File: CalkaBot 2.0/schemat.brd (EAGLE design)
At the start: 94.2 x 84.6 mm, 57 parts, among them IC1 TB6612FNG, IC2 LM339D, IC3 7806DT, Q1 16MHz

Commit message: end 3x
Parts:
- moved R11 14.4 mm to (8.20, 2.60)
- moved U$3 14.4 mm to (1.30, 2.50)
- moved R14 13.8 mm to (67.4, 2.60)
- moved U$2 13.8 mm to (74.4, 2.50)
- moved C6 13.6 mm to (23.6, 46.9)
- moved IC1 13.5 mm to (57.5, 57.9)
- moved LED3 13.5 mm to (65.1, 28.4)
- moved R10 13.5 mm to (65.3, 19.4)
- moved R8 13.5 mm to (72.1, 54.3)
- moved LED4 13.5 mm to (65.1, 24.2)
- moved R13 13.5 mm to (65.3, 21.5)
- moved C2 13.5 mm to (37.4, 9.72)
- moved C3 13.5 mm to (10.4, 43.1)
- moved IC3 13.5 mm to (15.0, 52.0)
- moved JP1 13.5 mm to (17.5, 57.2)
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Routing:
- net BO1: track 57.1 -> 105.2 mm
- net GND: track 481.3 -> 499.6 mm, vias 7 -> 8
- net VCC: track 432.6 -> 449.6 mm
- net FL3: track 43.5 -> 35.0 mm
- net I/O1: track 15.0 -> 8.22 mm
- net N$19: track 4.85 -> 10.8 mm
- net I/O2: track 14.5 -> 9.33 mm
- net AO2: track 19.6 -> 15.4 mm
- net N$1: track 8.38 -> 4.66 mm
- net I/O3: track 14.1 -> 10.5 mm
- net BO2: track 57.2 -> 59.7 mm
- net I/O4: track 13.6 -> 11.6 mm
- net I/O9: track 11.8 -> 12.9 mm
- net I/O6: track 12.7 -> 13.8 mm
- net S1: track 59.0 -> 59.6 mm
- added copper zone on layer 1, net N$3
- added copper zone on layer 16, net N$5
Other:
- board size 94.2 x 84.6 mm -> 76.8 x 68.7 mm
- board text added: "+"
- board text added: "A0"
- board text added: "A5"
- board text added: "C"
- board text added: "CałkaBot2.0"

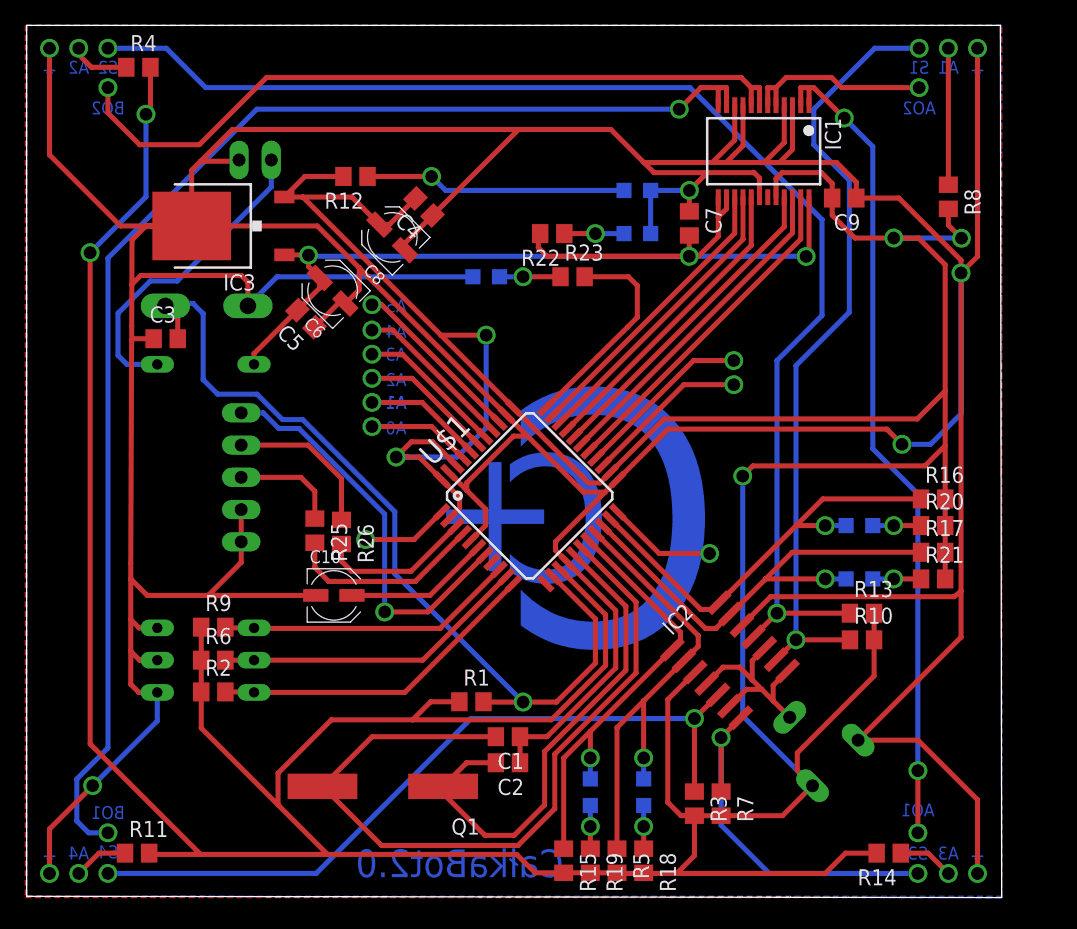
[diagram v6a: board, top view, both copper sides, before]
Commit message: poprawki wprowadzone, zmiana dipa z 3 na 4, przesunięcie włącznika zasilania
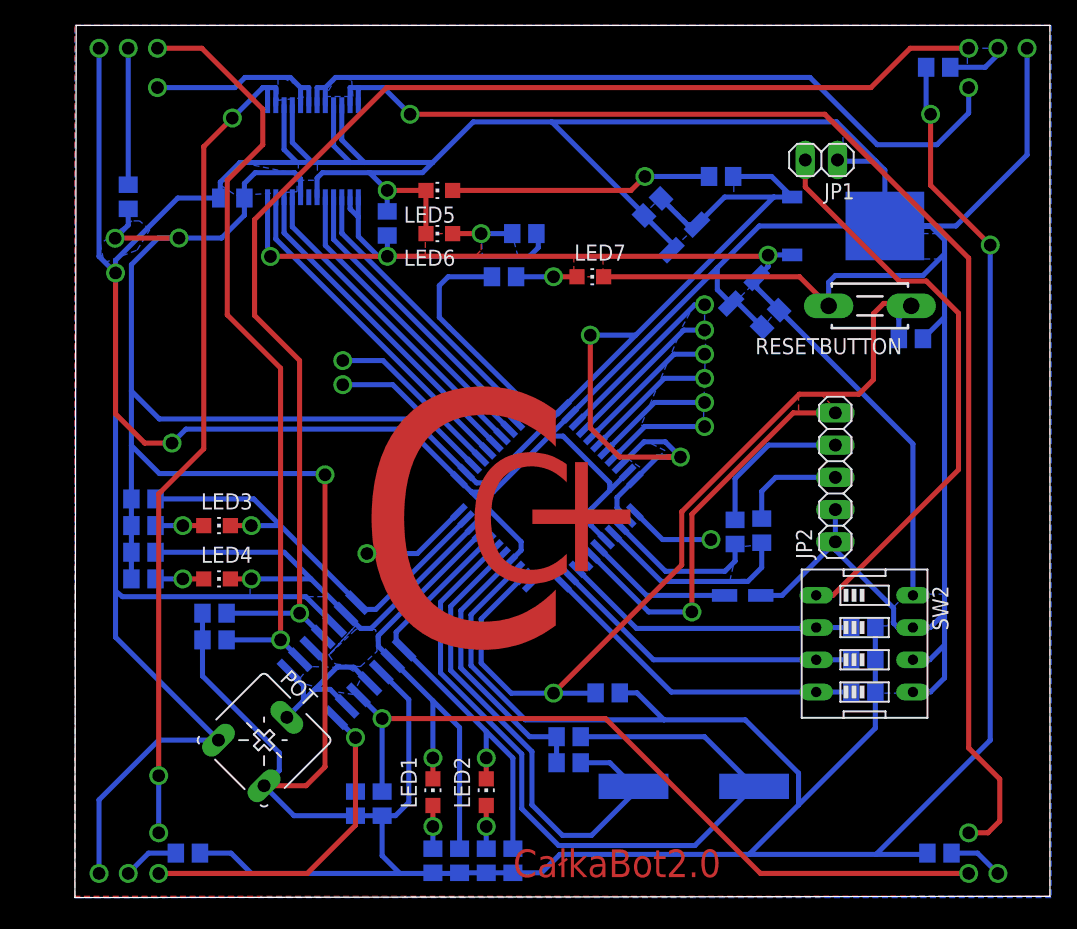
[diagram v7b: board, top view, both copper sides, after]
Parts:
- removed SW1: (no value), special:EDG-01
- removed U$2, U$3, U$4, U$5: (no value), untitled:GND@1
- SW2: device special:EDG-03 -> special:EDG-04
- moved R8 64.6 mm to (7.50, 54.3), flipped to the bottom
- moved R11 63.2 mm to (71.4, 2.60), flipped to the bottom
- moved R4 63.0 mm to (71.3, 64.5), flipped to the bottom
- moved R16 62.2 mm to (8.70, 30.5), flipped to the bottom
- moved R17 62.2 mm to (8.70, 26.3), flipped to the bottom
- moved R20 62.2 mm to (8.70, 28.4), flipped to the bottom
- moved R21 62.2 mm to (8.70, 24.2), flipped to the bottom
- moved C3 58.7 mm to (69.2, 43.1), flipped to the bottom
- moved R14 55.2 mm to (12.2, 2.60), flipped to the bottom
- moved RESETBUTTON 52.2 mm to (65.9, 45.7), flipped to the top
- moved SW2 51.9 mm to (65.5, 19.1), flipped to the top
- moved R2 51.2 mm to (65.4, 15.3), flipped to the bottom
- moved R6 51.2 mm to (65.4, 17.8), flipped to the bottom
- moved R9 51.2 mm to (65.4, 20.4), flipped to the bottom
- moved R10 51.0 mm to (14.3, 19.4), flipped to the bottom
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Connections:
- net GND: now also SW2.7; no longer SW2.4
- net MISO: now also SW2.4; no longer SW2.3
- net MOSI: now also SW2.3; no longer SW2.2
- net PIN: now also SW2.1; no longer SW1.1
- net SCK: now also SW2.2; no longer SW2.1
- net VM: now also SW2.8; no longer SW1.2
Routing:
- net VM: track 79.9 -> 101.1 mm
- net PIN: track 25.0 -> 46.0 mm
- net GND: track 499.6 -> 482.6 mm, vias 8 -> 6
- net VCC: track 449.6 -> 450.7 mm
- net RST: track 68.5 -> 67.7 mm
- added copper zone on layer 16, net N$14
- added copper zone on layer 16, net N$18
- added copper zone on layer 16, net N$20
- added copper zone on layer 16, net N$21
- added copper zone on layer 16, net N$22
- added copper zone on layer 16, net N$24
- added copper zone on layer 1, net N$25
- added copper zone on layer 16, net N$26
- added copper zone on layer 16, net N$28
- added copper zone on layer 16, net N$3
- added copper zone on layer 16, net N$32
- added copper zone on layer 16, net N$33
- added copper zone on layer 16, net N$34
- added copper zone on layer 16, net N$35
- added copper zone on layer 16, net N$36
- added copper zone on layer 16, net N$37
- added copper zone on layer 16, net N$38
- added copper zone on layer 16, net N$39
- added copper zone on layer 16, net N$40
- added copper zone on layer 1, net N$41
- added copper zone on layer 1, net N$42
- added copper zone on layer 16, net N$43
- added copper zone on layer 1, net N$5
- added copper zone on layer 16, net N$6
- added copper zone on layer 16, net N$8
- removed copper zone on layer 1, net N$3
- removed copper zone on layer 16, net N$5
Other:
- outline, holes or cut-outs redrawn
- board text removed: "A0"
- board text removed: "A1"
- board text removed: "A2"
- board text removed: "A3"
- board text removed: "A4"
- board text removed: "A5"
- board text removed: "AO1"
- board text removed: "AO2"
- board text removed: "BO1"
- board text removed: "BO2"
- board text removed: "S1"
- board text removed: "S2"
- board text removed: "S3"
- board text removed: "S4"

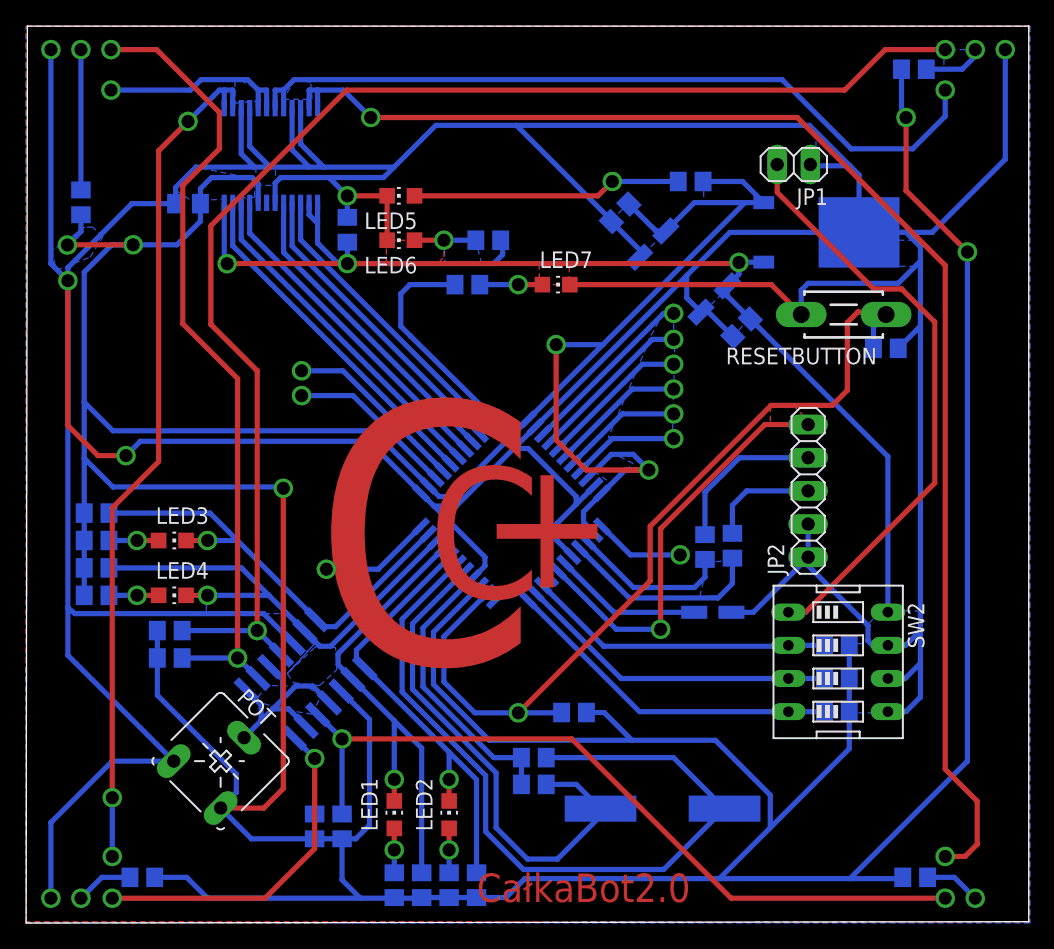
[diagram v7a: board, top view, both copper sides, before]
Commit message: dodałem gniazdo B, włącznik przyłączony z trybami
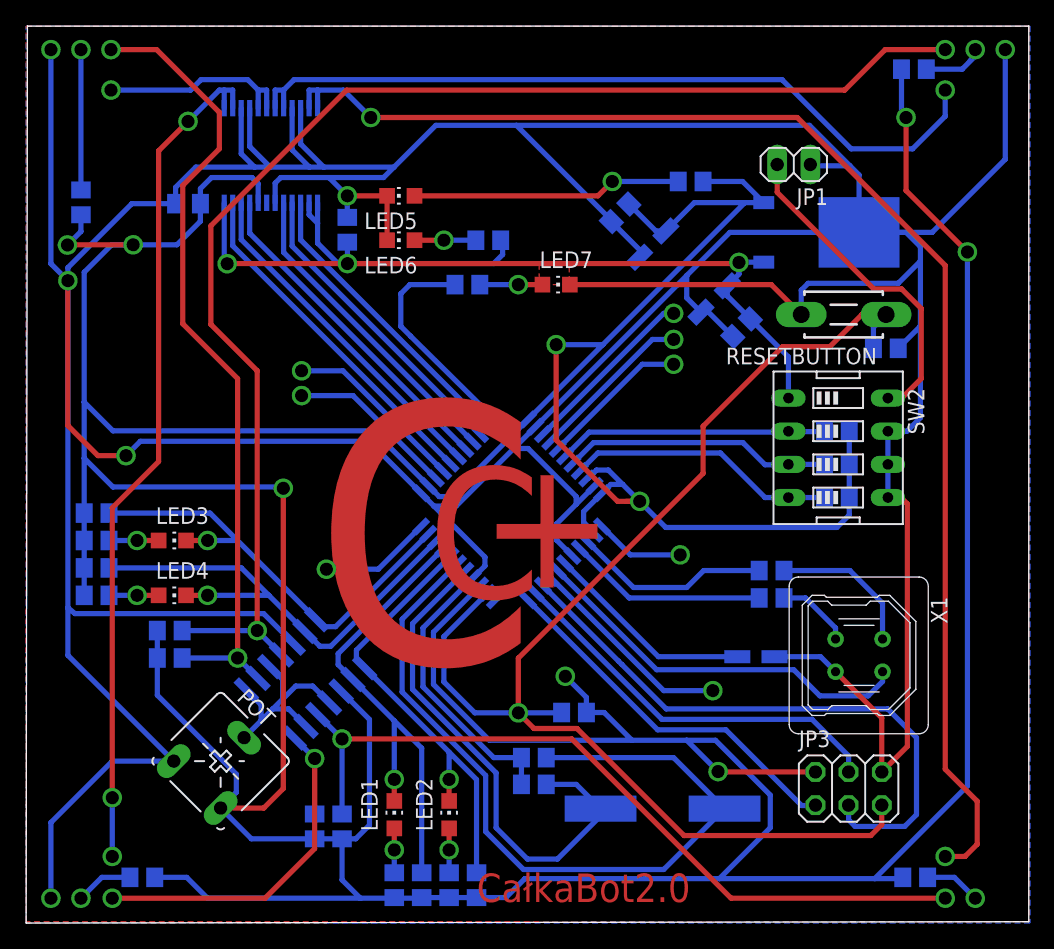
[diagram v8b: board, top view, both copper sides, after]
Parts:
- removed JP2: (no value), pinhead:1X05
- added JP3: (no value), pinhead:2X03
- added X1: MINI-USB_4P-85-32004-40X, con-cypressindustries:85-32004-40X
- moved R6 16.4 mm to (65.4, 34.2)
- moved R2 16.4 mm to (65.4, 31.7)
- moved R9 16.4 mm to (65.4, 36.8)
- moved SW2 16.4 mm to (65.5, 35.5)
- moved R26 5.41 mm to (60.4, 26.1), turned to 0 degrees
- moved R25 5.00 mm to (60.4, 24.0), turned to 0 degrees
- moved C10 4.74 mm to (59.2, 19.5)
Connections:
- new net I/O13: U$1.8
- net GND: now also JP3.6, X1.4; no longer JP2.1, JP2.2
- net I/O1: now also R2.2, SW2.4
- net I/O2: now also R6.2, SW2.3
- net I/O3: now also R9.2, SW2.2
- net MISO: now also JP3.1; no longer R2.2, SW2.4
- net MOSI: now also JP3.4; no longer R6.2, SW2.3
- net N$11: now also X1.2; no longer JP2.4
- net N$12: now also X1.3; no longer JP2.3
- net PIN: now also SW2.8; no longer SW2.1
- net RST: now also JP3.5
- net SCK: now also JP3.3; no longer R9.2, SW2.2
- net VBUS: now also X1.1; no longer JP2.5
- net VCC: now also JP3.2
- net VM: now also SW2.1; no longer SW2.8
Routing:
- net RST: track 67.7 -> 100.1 mm
- net SCK: track 24.0 -> 46.3 mm
- net PIN: track 46.0 -> 25.4 mm
- net VM: track 101.1 -> 81.5 mm
- net VCC: track 450.7 -> 468.6 mm, vias 7 -> 9
- net I/O13: track 0.00 -> 16.0 mm, vias 0 -> 1
- net I/O1: track 8.22 -> 20.7 mm, vias 1 -> 0
- net I/O2: track 9.33 -> 20.7 mm, vias 1 -> 0
- net I/O3: track 10.5 -> 20.8 mm, vias 1 -> 0
- net MOSI: track 24.9 -> 30.4 mm
- net GND: track 482.6 -> 477.5 mm
- net UCAP: track 11.4 -> 16.2 mm
- net D-: track 12.2 -> 15.2 mm
- net N$12: track 8.41 -> 5.75 mm
- net MISO: track 26.2 -> 28.5 mm
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- removed copper zone on layer 16, net N$14
- removed copper zone on layer 16, net N$18
- removed copper zone on layer 16, net N$20
- removed copper zone on layer 16, net N$21
- removed copper zone on layer 16, net N$22
- removed copper zone on layer 16, net N$24
- removed copper zone on layer 1, net N$25
- removed copper zone on layer 16, net N$26
- removed copper zone on layer 16, net N$28
- removed copper zone on layer 16, net N$32
- removed copper zone on layer 16, net N$33
- removed copper zone on layer 16, net N$34
- removed copper zone on layer 16, net N$35
- removed copper zone on layer 16, net N$36
- removed copper zone on layer 16, net N$37
- removed copper zone on layer 16, net N$38
- removed copper zone on layer 16, net N$39
- removed copper zone on layer 1, net N$41
- removed copper zone on layer 16, net N$43
- removed copper zone on layer 16, net N$6
- removed copper zone on layer 16, net N$8
